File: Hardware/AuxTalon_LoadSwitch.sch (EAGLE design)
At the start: 71 parts, among them J1 CONN_AUX_M12_REMOTE, J2 CONN_AUX_M12_REMOTE, J3 CONN_AUX_M12_REMOTE, J4 CONN_TALON_REMOTE, U1 ADS1115, U11 MCP23018QFN, U16 MAX9064, U17 MAX9064, U18 SN74AUP1T87, U19 MAX9064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

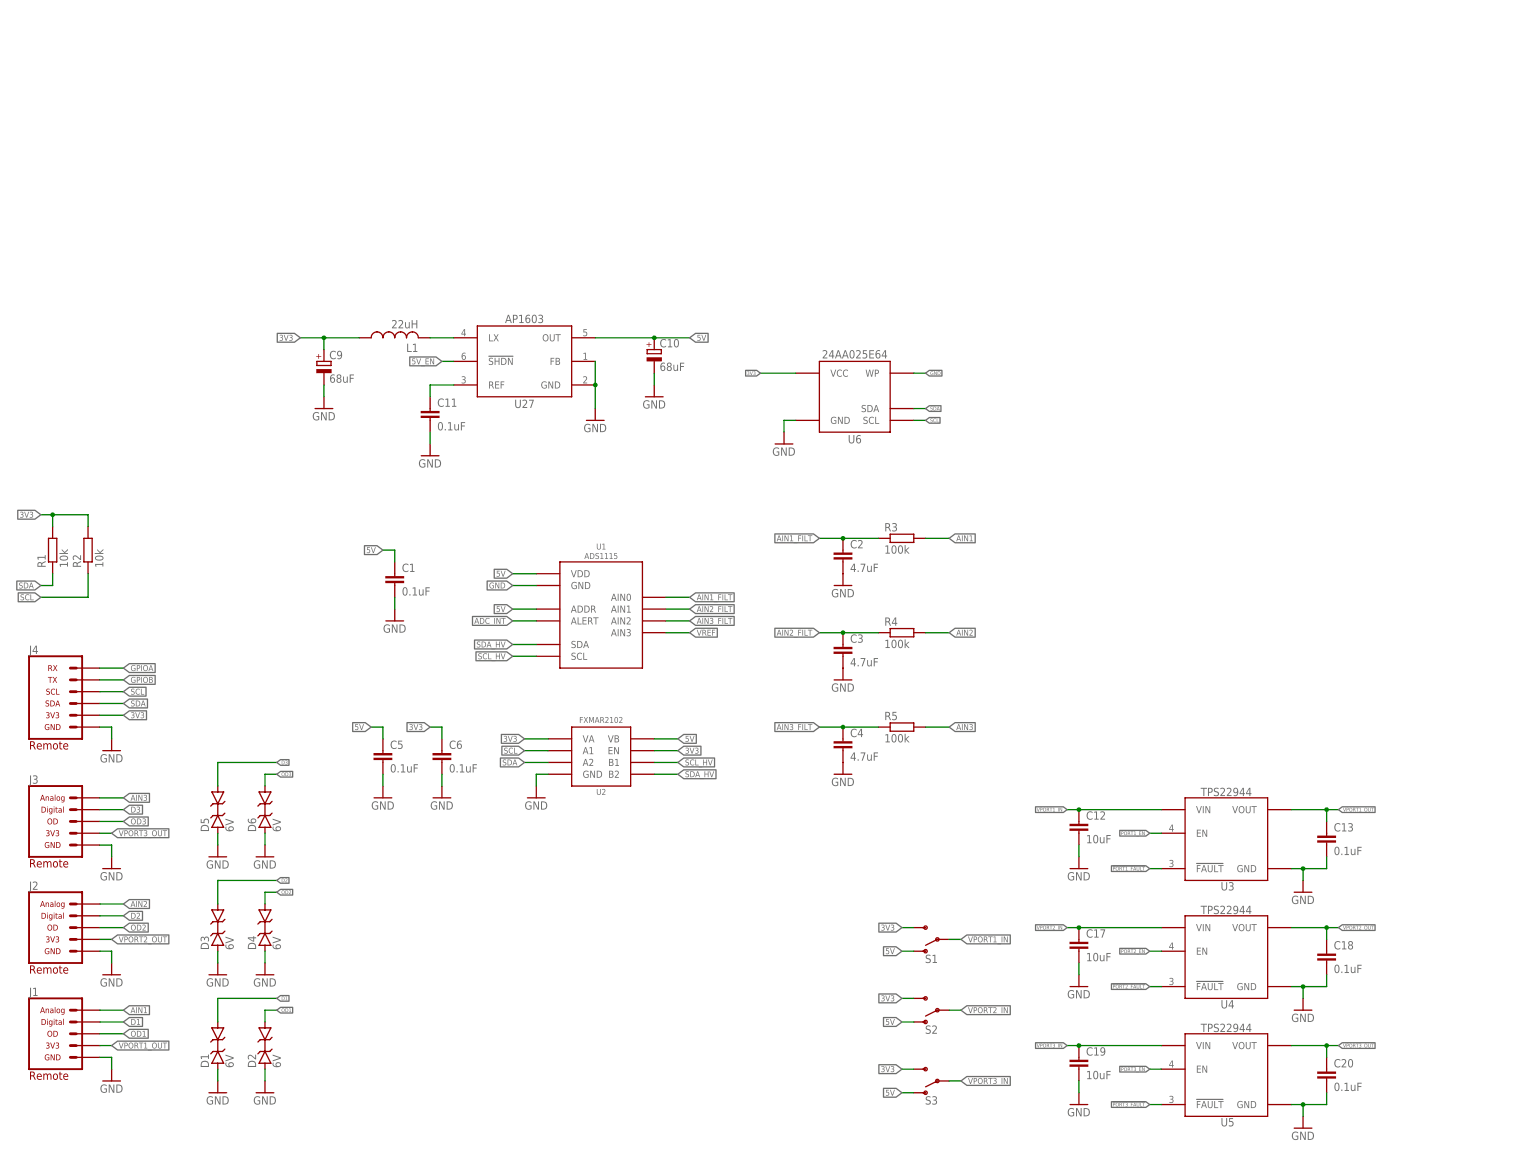
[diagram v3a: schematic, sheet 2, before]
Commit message: v1.0 Updates
Added voltage sensing for ports, swapped 5V converter, sent v1.0 to fab
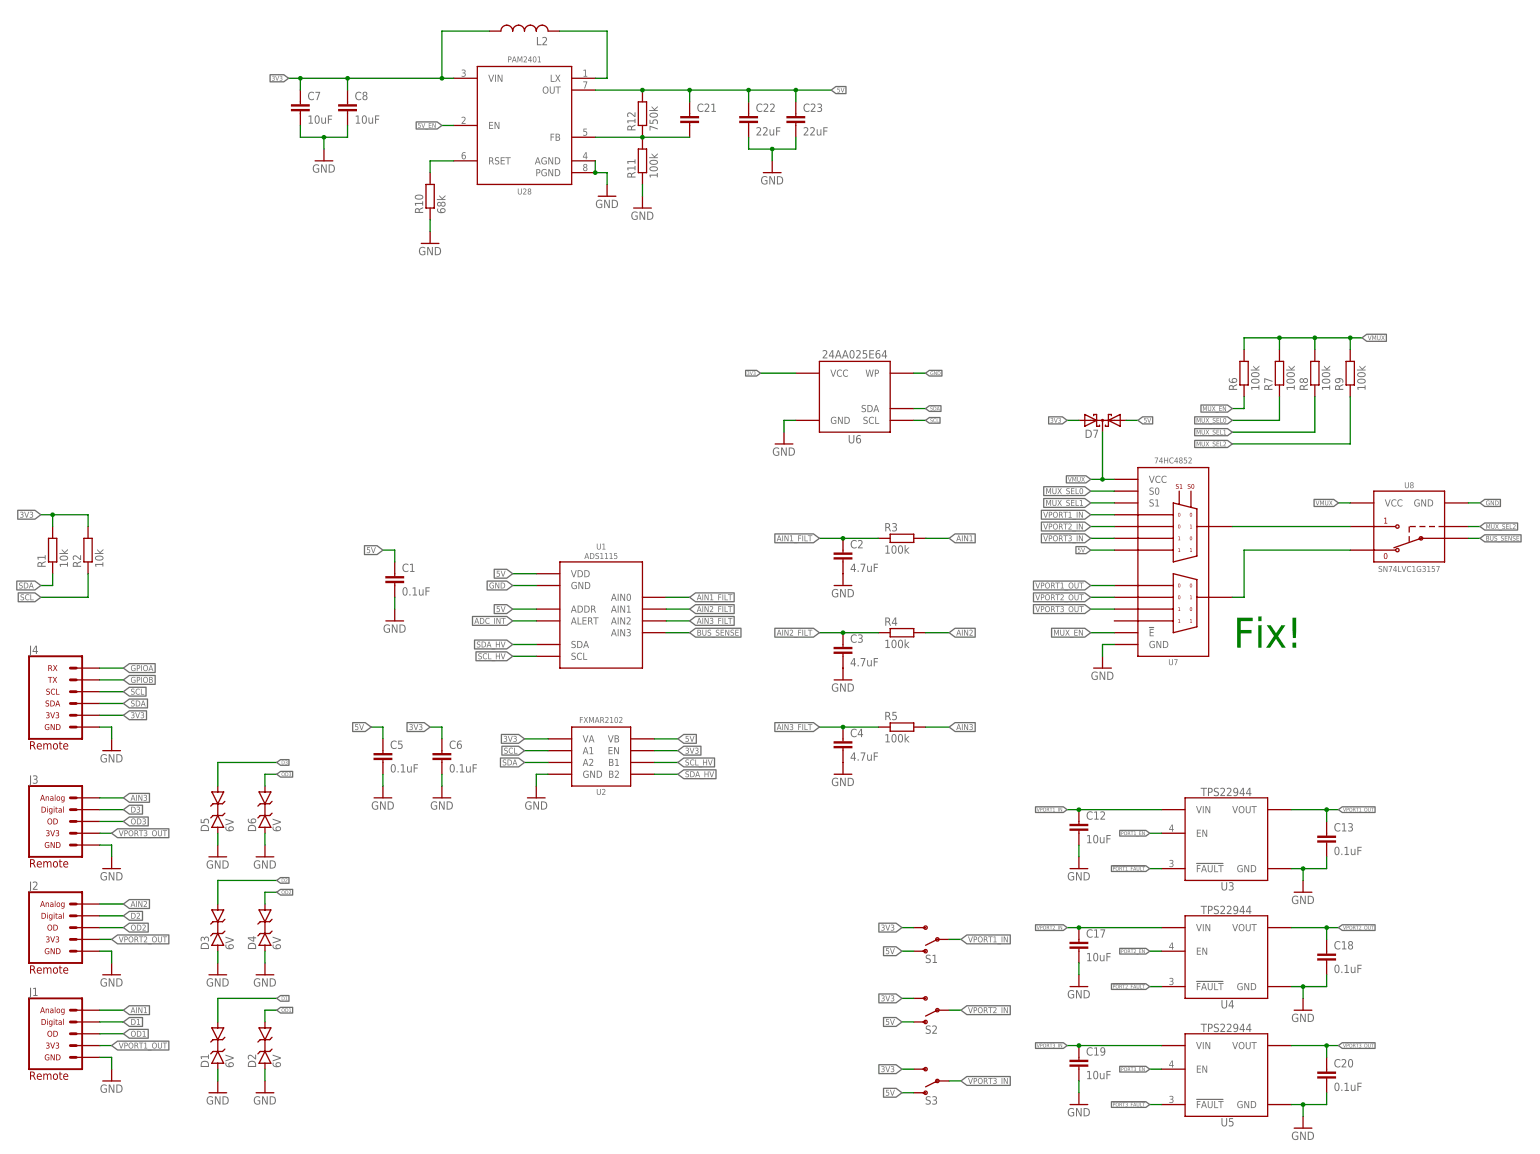
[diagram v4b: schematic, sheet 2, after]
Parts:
- removed C10, C9: 68uF, bschulz_passives:CPOL-EU153CLV-0605
- removed C11: 0.1uF, bschulz_passives:C-EU0.1UFC0402
- removed L1: 22uH, bschulz:INDUCTOR_TPC_3.8X3.8
- removed U27: AP1603, bschulz:AP1603
- added C21: (no value), bschulz_passives:C-EUC0402
- added C22, C23: 22uF, bschulz_passives:C-EU22UFC0805
- added C7, C8: 10uF, bschulz_passives:C-EU10UFC0805
- added D7: (no value), bschulz:DIODE_CCBAT54CSOT23
- added L2: (no value), bschulz:INDUCTOR_MAPI_2.5X2
- added R10: 68k, bschulz_passives:R-EU_R0603
- added R11: 100k, bschulz_passives:R-EU_100KR0603
- added R12: 750k, bschulz_passives:R-EU_750KR0603
- added R6, R7, R8, R9: 100k, bschulz_passives:R-EU_100KR0402
- added U28: PAM2401MSOP, bschulz:PAM2401MSOP
- added U7: 74HC4852, bschulz:74HC4852
- added U8: SN74LVC1G3157SC70, bschulz:SN74LVC1G3157SC70
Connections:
- removed net N$15: C11.1, U27.REF
- removed net N$17: L1.2, U27.LX
- removed net N$26: U25.GPB3
- removed net N$29: U25.GPB6
- removed net N$30: U25.GPB7
- removed net VREF: U1.AIN3
- new net BUS_SENSE: U1.AIN3, U8.A
- new net MUX_EN: R6.1, U26.GPB3, U7.!E
- new net MUX_SEL0: R7.1, U26.GPB0, U7.S0
- new net MUX_SEL1: R8.1, U26.GPB1, U7.S1
- new net N$1: U7.2Z, U8.B1
- new net N$18: L2.2, U28.LX
- new net N$2: R10.2, U28.RSET
- new net N$3: C21.2, R11.2, R12.1, U28.FB
- new net N$38: U7.1Z, U8.B2
- new net VMUX: D7.C, R6.2, R7.2, R8.2, R9.2, U7.VCC, U8.VCC
- net 3V3: now also C7.1, C8.1, D7.A2, L2.1, U28.VIN; no longer C9.+, L1.1
- net 5V: now also C21.1, C22.1, C23.1, D7.A1, R12.2, U28.OUT, U7.1Y3; no longer C10.+, U27.OUT
- net 5V_EN: now also U28.EN; no longer U27.!SHDN
- net GND: now also C22.2, C23.2, C7.2, C8.2, R10.1, R11.1, U28.AGND, U28.PGND, U7.GND, U8.GND; no longer C10.-, C11.2, C9.-, U27.FB, U27.GND
- net MUX_SEL2: now also R9.1, U26.GPB2, U8.S; no longer U25.GPB5
- net VPORT1_IN: now also U7.1Y0
- net VPORT1_OUT: now also U7.2Y0
- net VPORT2_IN: now also U7.1Y1
- net VPORT2_OUT: now also U7.2Y1
- net VPORT3_IN: now also U7.1Y2
- net VPORT3_OUT: now also U7.2Y2
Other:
- note added: "Fix!"

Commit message: Update part val, generated BoM for v1.0
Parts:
- L2: value (none) -> 4.7uH
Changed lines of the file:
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@@
 <part name="GND52" library="supply1" library_urn="urn:adsk.eagle:library:371" deviceset="GND" device=""/>
 <part name="GND53" library="supply1" library_urn="urn:adsk.eagle:library:371" deviceset="GND" device=""/>
-<part name="L2" library="bschulz" deviceset="INDUCTOR" device="_MAPI_2.5X2"/>
+<part name="L2" library="bschulz" deviceset="INDUCTOR" device="_MAPI_2.5X2" value="4.7uH"/>
 <part name="R11" library="bschulz_passives" deviceset="R-EU_" device="R0603" technology="100K" value="100k"/>
 <part name="R12" library="bschulz_passives" deviceset="R-EU_" device="R0603" technology="750K" value="750k"/>

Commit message: Prelim v1.3 updates
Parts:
- added C10, C11, C9: (no value), bschulz_passives:C-EUC0402
- added R13, R23, R24: (no value), bschulz_passives:R-EU_100KR0402
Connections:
- net D1: now also R13.2
- net D2: now also R23.2
- net D3: now also R24.2
- net GND: now also C10.2, C11.2, C9.2, R13.1, R23.1, R24.1
- net OD1: now also C11.1
- net OD2: now also C10.1
- net OD3: now also C9.1
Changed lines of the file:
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@@
 <part name="C23" library="bschulz_passives" deviceset="C-EU" device="C0805" technology="22UF" value="22uF"/>
 <part name="GND55" library="supply1" library_urn="urn:adsk.eagle:library:371" deviceset="GND" device=""/>
+<part name="C9" library="bschulz_passives" deviceset="C-EU" device="C0402"/>
+<part name="C10" library="bschulz_passives" deviceset="C-EU" device="C0402"/>
+<part name="C11" library="bschulz_passives" deviceset="C-EU" device="C0402"/>
+<part name="R13" library="bschulz_passives" deviceset="R-EU_" device="R0402" technology="100K"/>
+<part name="R23" library="bschulz_passives" deviceset="R-EU_" device="R0402" technology="100K"/>
+<part name="R24" library="bschulz_passives" deviceset="R-EU_" device="R0402" technology="100K"/>
+<part name="GND46" library="supply1" library_urn="urn:adsk.eagle:library:371" deviceset="GND" device=""/>
+<part name="GND47" library="supply1" library_urn="urn:adsk.eagle:library:371" deviceset="GND" device=""/>
+<part name="GND48" library="supply1" library_urn="urn:adsk.eagle:library:371" deviceset="GND" device=""/>
 </parts>
 <sheets>
@@
 <attribute name="VALUE" x="172.72" y="213.36" size="1.778" layer="96"/>
 </instance>
+<instance part="C9" gate="G$1" x="88.9" y="68.58" smashed="yes">
+<attribute name="NAME" x="90.424" y="68.961" size="1.778" layer="95"/>
+<attribute name="VALUE" x="90.424" y="63.881" size="1.778" layer="96"/>
+</instance>
+<instance part="C10" gate="G$1" x="88.9" y="50.8" smashed="yes">
+<attribute name="NAME" x="90.424" y="51.181" size="1.778" layer="95"/>
+<attribute name="VALUE" x="90.424" y="46.101" size="1.778" layer="96"/>
+</instance>
+<instance part="C11" gate="G$1" x="88.9" y="30.48" smashed="yes">
+<attribute name="NAME" x="90.424" y="30.861" size="1.778" layer="95"/>
+<attribute name="VALUE" x="90.424" y="25.781" size="1.778" layer="96"/>
+</instance>
+<instance part="R13" gate="G$1" x="106.68" y="27.94" smashed="yes" rot="R90">
+<attribute name="NAME" x="105.1814" y="24.13" size="1.778" layer="95" rot="R90"/>
+<attribute name="VALUE" x="109.982" y="24.13" size="1.778" layer="96" rot="R90"/>
+</instance>
+<instance part="R23" gate="G$1" x="106.68" y="48.26" smashed="yes" rot="R90">
+<attribute name="NAME" x="105.1814" y="44.45" size="1.778" layer="95" rot="R90"/>
+<attribute name="VALUE" x="109.982" y="44.45" size="1.778" layer="96" rot="R90"/>
+</instance>
+<instance part="R24" gate="G$1" x="106.68" y="66.04" smashed="yes" rot="R90">
+<attribute name="NAME" x="105.1814" y="62.23" size="1.778" layer="95" rot="R90"/>
+<attribute name="VALUE" x="109.982" y="62.23" size="1.778" layer="96" rot="R90"/>
+</instance>
+<instance part="GND46" gate="1" x="88.9" y="20.32" smashed="yes">
+<attribute name="VALUE" x="86.36" y="17.78" size="1.778" layer="96"/>
+</instance>
+<instance part="GND47" gate="1" x="88.9" y="40.64" smashed="yes">
+<attribute name="VALUE" x="86.36" y="38.1" size="1.778" layer="96"/>
+</instance>
+<instance part="GND48" gate="1" x="88.9" y="58.42" smashed="yes">
+<attribute name="VALUE" x="86.36" y="55.88" size="1.778" layer="96"/>
+</instance>
 </instances>
 <busses>
@@
 <junction x="175.26" y="220.98"/>
 <pinref part="GND55" gate="1" pin="GND"/>
+</segment>
+<segment>
+<pinref part="GND48" gate="1" pin="GND"/>
+<pinref part="C9" gate="G$1" pin="2"/>
+<wire x1="88.9" y1="60.96" x2="88.9" y2="63.5" width="0.1524" layer="91"/>
+<pinref part="R24" gate="G$1" pin="1"/>
+<wire x1="88.9" y1="60.96" x2="106.68" y2="60.96" width="0.1524" layer="91"/>
+<junction x="88.9" y="60.96"/>
+</segment>
+<segment>
+<pinref part="R23" gate="G$1" pin="1"/>
+<pinref part="GND47" gate="1" pin="GND"/>
+<wire x1="106.68" y1="43.18" x2="88.9" y2="43.18" width="0.1524" layer="91"/>
+<pinref part="C10" gate="G$1" pin="2"/>
+<wire x1="88.9" y1="43.18" x2="88.9" y2="45.72" width="0.1524" layer="91"/>
+<junction x="88.9" y="43.18"/>
+</segment>
+<segment>
+<pinref part="R13" gate="G$1" pin="1"/>
+<pinref part="GND46" gate="1" pin="GND"/>
+<wire x1="106.68" y1="22.86" x2="88.9" y2="22.86" width="0.1524" layer="91"/>
+<pinref part="C11" gate="G$1" pin="2"/>
+<wire x1="88.9" y1="22.86" x2="88.9" y2="25.4" width="0.1524" layer="91"/>
+<junction x="88.9" y="22.86"/>
 </segment>
 </net>
@@
 <label x="68.58" y="38.1" size="0.8128" layer="95" xref="yes"/>
 </segment>
+<segment>
+<pinref part="R13" gate="G$1" pin="2"/>
+<wire x1="106.68" y1="33.02" x2="109.22" y2="33.02" width="0.1524" layer="91"/>
+<label x="109.22" y="33.02" size="1.27" layer="95" xref="yes"/>
+</segment>
 </net>
 <net name="OD1" class="0">
@@
 <label x="68.58" y="35.56" size="0.8128" layer="95" xref="yes"/>
 </segment>
+<segment>
+<pinref part="C11" gate="G$1" pin="1"/>
+<wire x1="88.9" y1="33.02" x2="86.36" y2="33.02" width="0.1524" layer="91"/>
+<label x="86.36" y="33.02" size="1.27" layer="95" rot="R180" xref="yes"/>
+</segment>
 </net>
 <net name="D3" class="0">
@@
 <label x="68.58" y="88.9" size="0.8128" layer="95" xref="yes"/>
 </segment>
+<segment>
+<pinref part="R24" gate="G$1" pin="2"/>
+<wire x1="106.68" y1="71.12" x2="109.22" y2="71.12" width="0.1524" layer="91"/>
+<label x="109.22" y="71.12" size="1.27" layer="95" xref="yes"/>
+</segment>
 </net>
 <net name="OD3" class="0">
@@
 <label x="68.58" y="86.36" size="0.8128" layer="95" xref="yes"/>
 </segment>
+<segment>
+<pinref part="C9" gate="G$1" pin="1"/>
+<wire x1="88.9" y1="71.12" x2="86.36" y2="71.12" width="0.1524" layer="91"/>
+<label x="86.36" y="71.12" size="1.27" layer="95" rot="R180" xref="yes"/>
+</segment>
 </net>
 <net name="D2" class="0">
@@
 <label x="68.58" y="63.5" size="0.8128" layer="95" xref="yes"/>
 </segment>
+<segment>
+<pinref part="R23" gate="G$1" pin="2"/>
+<wire x1="106.68" y1="53.34" x2="109.22" y2="53.34" width="0.1524" layer="91"/>
+<label x="109.22" y="53.34" size="1.27" layer="95" xref="yes"/>
+</segment>
 </net>
 <net name="OD2" class="0">
@@
 <label x="68.58" y="60.96" size="0.8128" layer="95" xref="yes"/>
 </segment>
-</net>
+<segment>
+<pinref part="C10" gate="G$1" pin="1"/>
+<wire x1="88.9" y1="53.34" x2="86.36" y2="53.34" width="0.1524" layer="91"/>
+<label x="86.36" y="53.34" size="1.27" layer="95" rot="R180" xref="yes"/>
+</segment>
+</net>
